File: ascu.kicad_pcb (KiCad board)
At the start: 2 copper layers, 109.6 x 35.9 mm, 91 parts, among them IC1 ATTINY25-SS, P1 B-, P10 CONN_01X01, P11 CONN_01X01, P12 CONN_01X01, P13 CONN_01X01, P14 CONN_01X01, P15 CONN_01X01, P16 CONN_01X01, P17 CONN_01X01, P18 CONN_01X01, P19 CONN_01X01, P2 B+S+, P20 CONN_01X01, P21 CONN_01X01, P22 CONN_01X01, P23 CONN_01X01, P24 CONN_01X01, P25 CONN_01X01, P26 CONN_01X01, P27 CONN_01X01, P28 CONN_01X01, P29 CONN_01X01, P3 S-, P30 CONN_01X01, P31 CONN_01X01, P32 CONN_01X01, P33 CONN_01X01, P34 CONN_01X01, P35 CONN_01X01, P37 Otwór, P38 Otwór, P39 Otwór, P4 CONN_01X01, P40 Otwór, P41 Lut, P42 Lut, P43 Lut, P44 Lut, P45 Lut, P46 Lut, P47 Lut, P48 Lut, P49 Lut, P5 CONN_01X01, P50 Lut, P51 Lut, P52 Lut, P53 Lut, P54 Lut, P55 Lut, P56 Lut, P6 CONN_01X01, P7 CONN_01X01, P8 CONN_01X01, P9 CONN_01X01, Q1 PSMN1R2, Q2 PSMN1R2, SW1 DETECT, SW3 TRIGGER, U1 SPX3819, U2 MIC4605, U3 TLP291

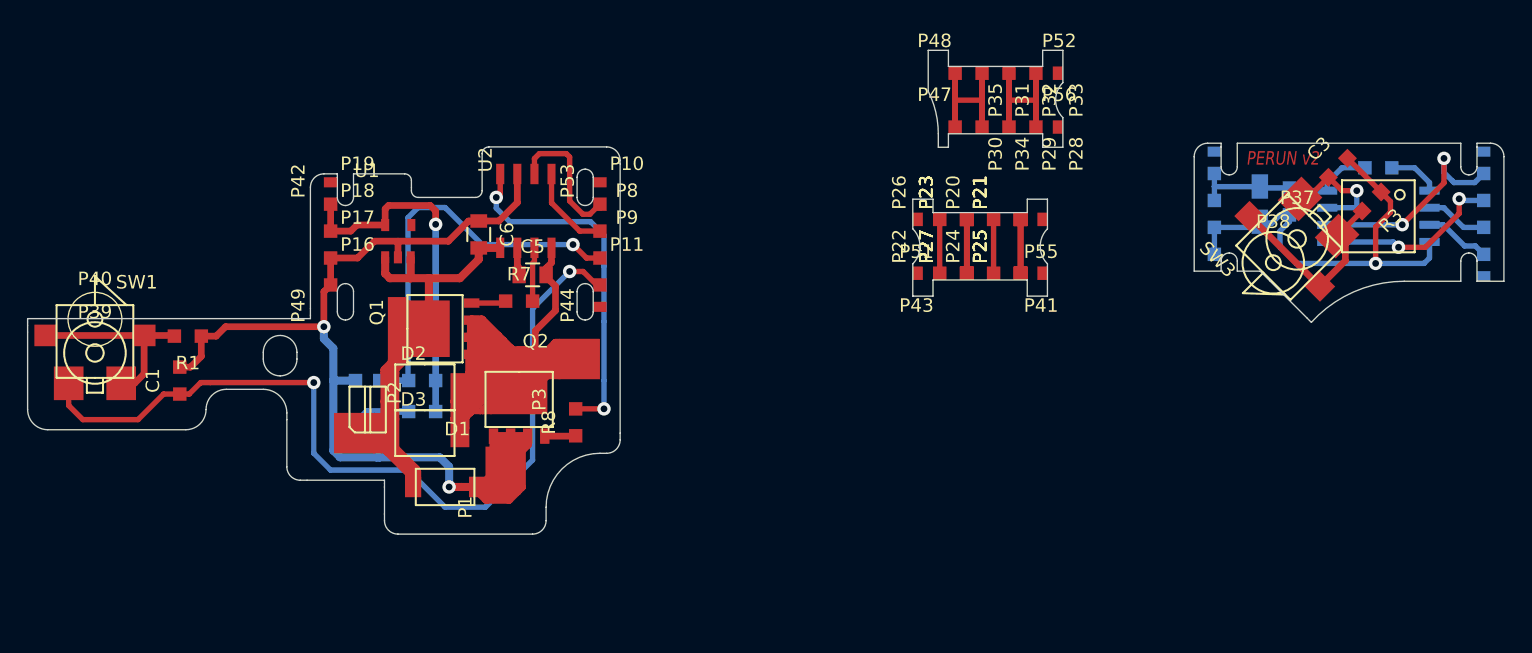
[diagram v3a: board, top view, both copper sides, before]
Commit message: Revert "Poprawki"
This reverts commit 9021c68e6a4ef5e3f9d6ce24ccd05bc863d9a415.
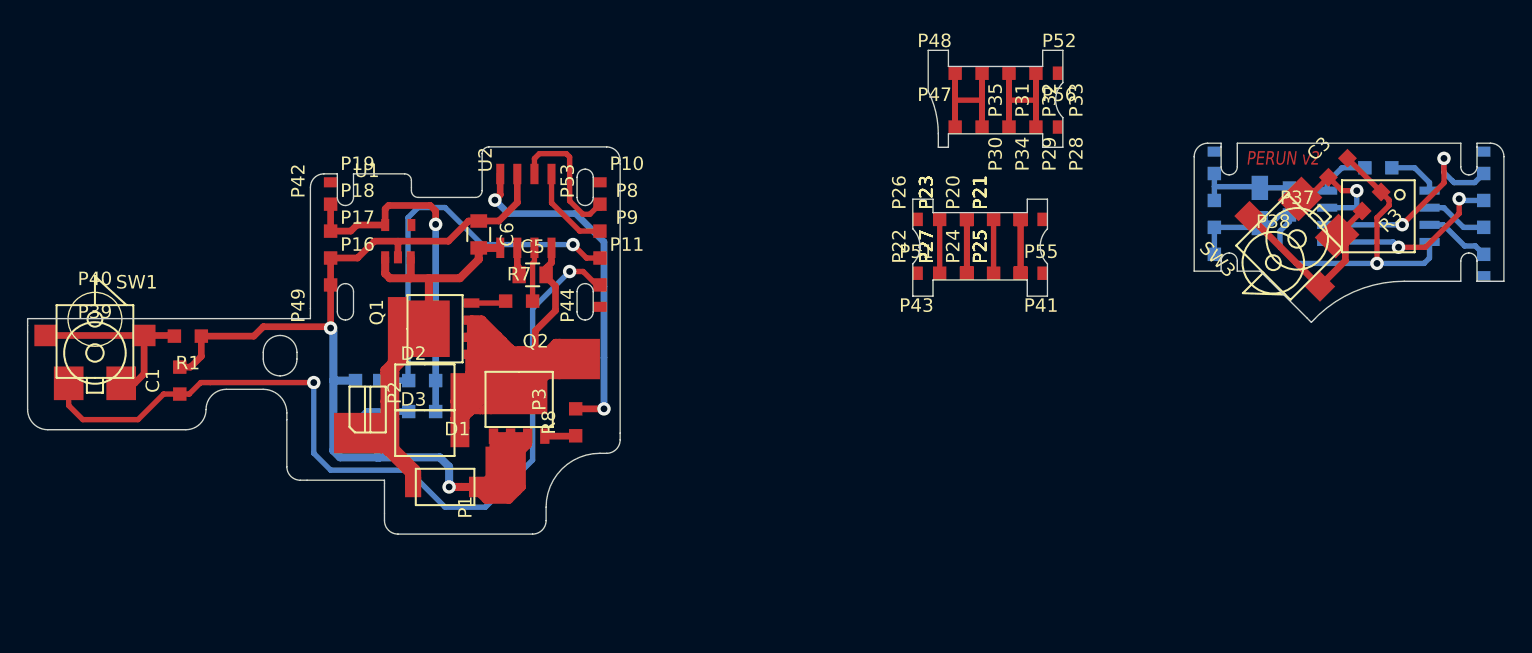
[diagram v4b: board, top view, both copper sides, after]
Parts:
- moved C2 0.10 mm to (200.5, 73.1)
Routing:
- net LO: track 26.5 -> 26.0 mm
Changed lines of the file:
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@@
     (links 93)
     (no_connects 0)
-    (area 108.899999 58.4 227.783334 97.550001)
+    (area 108.899999 58.4 198.783334 110.600001)
     (thickness 1)
     (drawings 181)
-    (tracks 478)
+    (tracks 475)
     (zones 0)
     (modules 91)
@@
   )
   (module Capacitors_Tantalum_SMD:TantalC_SizeA_EIA-3216_Reflow (layer B.Cu)
-    (at 200.5 73 270)
+    (at 200.5 73.1 270)
     (descr "Tantal Cap. , Size A, EIA-3216, Reflow")
     (tags "Tantal Capacitor Size-A EIA-3216 reflow")
@@
   (gr_line (start 128 81) (end 128 78.5) (angle 90) (layer Margin) (width 0.2))
   (gr_line (start 130 81) (end 128 81) (angle 90) (layer Margin) (width 0.2))
-  (segment (start 131 82.1) (end 131 83) (width 0.6) (layer B.Cu) (net 1))
-  (via (at 131 82.1) (size 1) (drill 0.5) (layers F.Cu B.Cu) (net 1))
-  (segment (start 131.7 83.7) (end 131.7 86.1) (width 0.6) (layer B.Cu) (net 1))
-  (segment (start 131 83) (end 131.7 83.7) (width 0.6) (layer B.Cu) (net 1))
-  (segment (start 131 82.1) (end 131 79.5) (width 0.5) (layer F.Cu) (net 1))
-  (segment (start 123 82.8) (end 123.7 82.1) (width 0.5) (layer F.Cu) (net 1))
-  (segment (start 123.7 82.1) (end 131 82.1) (width 0.5) (layer F.Cu) (net 1))
-  (segment (start 121.9 82.8) (end 123 82.8) (width 0.5) (layer F.Cu) (net 1) (status 400000))
-  (segment (start 131 79.5) (end 131.5 79) (width 0.5) (layer F.Cu) (net 1) (status 800000))
   (segment (start 120.3 85.1) (end 121.1 85.1) (width 0.5) (layer F.Cu) (net 1))
+  (segment (start 121.9 84.3) (end 121.9 82.8) (width 0.5) (layer F.Cu) (net 1))
   (segment (start 121.1 85.1) (end 121.9 84.3) (width 0.5) (layer F.Cu) (net 1))
-  (segment (start 121.9 84.3) (end 121.9 82.8) (width 0.5) (layer F.Cu) (net 1))
+  (segment (start 121.9 82.8) (end 125.8 82.8) (width 0.5) (layer F.Cu) (net 1))
+  (segment (start 131.4 82.1) (end 131.5 82.2) (width 0.5) (layer F.Cu) (net 1))
+  (segment (start 126.5 82.1) (end 131.4 82.1) (width 0.5) (layer F.Cu) (net 1))
+  (segment (start 125.8 82.8) (end 126.5 82.1) (width 0.5) (layer F.Cu) (net 1))
   (segment (start 135.15 90.4) (end 135.15 91.8) (width 0.6) (layer B.Cu) (net 1))
   (segment (start 135.15 91.8) (end 134.9 91.8) (width 0.6) (layer B.Cu) (net 1))
@@
   (segment (start 131.7 86.1) (end 131.9 86.1) (width 0.6) (layer B.Cu) (net 1))
   (segment (start 131.9 86.1) (end 131.7 86.1) (width 0.6) (layer B.Cu) (net 1))
+  (segment (start 131.5 82.2) (end 131.5 82.25) (width 0.6) (layer F.Cu) (net 1))
+  (segment (start 131.5 79) (end 131.5 82.25) (width 0.5) (layer F.Cu) (net 1))
+  (via (at 131.5 82.2) (size 1) (drill 0.5) (layers F.Cu B.Cu) (net 1))
+  (segment (start 131.7 86.1) (end 131.7 82.4) (width 0.6) (layer B.Cu) (net 1))
+  (segment (start 131.7 82.4) (end 131.5 82.2) (width 0.6) (layer B.Cu) (net 1))
   (segment (start 131.7 91.3) (end 131.7 86.1) (width 0.6) (layer B.Cu) (net 1))
+  (segment (start 134.9 91.8) (end 132.2 91.8) (width 0.6) (layer B.Cu) (net 1))
   (segment (start 132.2 91.8) (end 131.7 91.3) (width 0.6) (layer B.Cu) (net 1))
-  (segment (start 134.9 91.8) (end 132.2 91.8) (width 0.6) (layer B.Cu) (net 1))
   (segment (start 142.375 94) (end 143 94) (width 1.2) (layer F.Cu) (net 1))
   (segment (start 143 94) (end 144.5 92.5) (width 1.2) (layer F.Cu) (net 1))
@@
   (segment (start 203.656371 72.635913) (end 203.664087 72.635913) (width 0.4) (layer F.Cu) (net 11))
   (segment (start 205.5 71.995) (end 202.895 71.995) (width 0.4) (layer B.Cu) (net 12))
+  (segment (start 202.895 71.995) (end 202.7 71.8) (width 0.4) (layer B.Cu) (net 12))
   (segment (start 200.5 71.79) (end 202.69 71.79) (width 0.4) (layer B.Cu) (net 12))
+  (segment (start 202.69 71.79) (end 202.7 71.8) (width 0.4) (layer B.Cu) (net 12))
   (segment (start 197.125 71.7) (end 200.41 71.7) (width 0.4) (layer B.Cu) (net 12))
   (segment (start 200.41 71.7) (end 200.5 71.79) (width 0.4) (layer B.Cu) (net 12))
-  (segment (start 202.895 71.995) (end 202.7 71.8) (width 0.4) (layer B.Cu) (net 12))
-  (segment (start 202.69 71.79) (end 202.7 71.8) (width 0.4) (layer B.Cu) (net 12))
   (segment (start 197.125 72.725) (end 197.125 71.7) (width 0.4) (layer B.Cu) (net 12))
   (segment (start 197.125 71.7) (end 197.125 70.725) (width 0.4) (layer B.Cu) (net 12))
@@
   (segment (start 205.5 71.4) (end 205.5 71.995) (width 0.4) (layer B.Cu) (net 12))
   (segment (start 206.6 70.3) (end 205.5 71.4) (width 0.4) (layer B.Cu) (net 12))
-  (segment (start 209.507107 72.092893) (end 209.507107 72.107107) (width 0.4) (layer F.Cu) (net 13) (status C00000))
-  (segment (start 209.507107 72.107107) (end 210.2 72.8) (width 0.4) (layer F.Cu) (net 13) (status 400000))
-  (segment (start 209.1 77.4) (end 209.2 77.4) (width 0.4) (layer B.Cu) (net 13))
-  (via (at 209.1 77.4) (size 1) (drill 0.5) (layers F.Cu B.Cu) (net 13))
-  (segment (start 209.1 74.7) (end 209.1 77.4) (width 0.4) (layer F.Cu) (net 13))
-  (segment (start 210.2 73.6) (end 209.1 74.7) (width 0.4) (layer F.Cu) (net 13))
-  (segment (start 210.2 72.8) (end 210.2 73.6) (width 0.4) (layer F.Cu) (net 13))
-  (segment (start 200.5 74.41) (end 201.39 74.41) (width 0.4) (layer B.Cu) (net 13))
-  (segment (start 201.39 74.41) (end 202 73.8) (width 0.4) (layer B.Cu) (net 13))
-  (segment (start 202 73.8) (end 202.7 73.8) (width 0.4) (layer B.Cu) (net 13))
-  (segment (start 197.125 74.725) (end 200.185 74.725) (width 0.4) (layer B.Cu) (net 13))
+  (segment (start 209.507107 72.092893) (end 209.507107 72.107107) (width 0.4) (layer F.Cu) (net 13))
+  (segment (start 209.507107 72.107107) (end 210.1 72.7) (width 0.4) (layer F.Cu) (net 13))
+  (via (at 209.2 77.4) (size 1) (drill 0.5) (layers F.Cu B.Cu) (net 13))
+  (segment (start 209.2 74) (end 209.2 77.4) (width 0.4) (layer F.Cu) (net 13))
+  (segment (start 210.1 73.1) (end 209.2 74) (width 0.4) (layer F.Cu) (net 13))
+  (segment (start 210.1 72.7) (end 210.1 73.1) (width 0.4) (layer F.Cu) (net 13))
+  (segment (start 209.507107 72.092893) (end 207.007107 69.592893) (width 0.4) (layer F.Cu) (net 13))
+  (segment (start 202.7 73.8) (end 202.7 74.3) (width 0.4) (layer B.Cu) (net 13))
   (segment (start 202.7 74.3) (end 202 75) (width 0.4) (layer B.Cu) (net 13))
-  (segment (start 202 75) (end 202 76.2) (width 0.4) (layer B.Cu) (net 13))
-  (segment (start 202 76.2) (end 203.2 77.4) (width 0.4) (layer B.Cu) (net 13))
-  (segment (start 203.2 77.4) (end 209.2 77.4) (width 0.4) (layer B.Cu) (net 13))
-  (segment (start 202.7 73.8) (end 202.7 74.3) (width 0.4) (layer B.Cu) (net 13))
-  (segment (start 200.185 74.725) (end 200.5 74.41) (width 0.4) (layer B.Cu) (net 13))
-  (segment (start 209.507107 72.092893) (end 207.007107 69.592893) (width 0.4) (layer F.Cu) (net 13))
   (segment (start 213.1 77) (end 213.1 75.805) (width 0.4) (layer B.Cu) (net 13))
   (segment (start 212.7 77.4) (end 213.1 77) (width 0.4) (layer B.Cu) (net 13))
+  (segment (start 203.2 77.4) (end 209.2 77.4) (width 0.4) (layer B.Cu) (net 13))
   (segment (start 209.2 77.4) (end 212.7 77.4) (width 0.4) (layer B.Cu) (net 13))
+  (segment (start 202 76.2) (end 203.2 77.4) (width 0.4) (layer B.Cu) (net 13))
+  (segment (start 202 75) (end 202 76.2) (width 0.4) (layer B.Cu) (net 13))
+  (segment (start 200.5 74.41) (end 201.39 74.41) (width 0.4) (layer B.Cu) (net 13))
+  (segment (start 202 73.8) (end 202.7 73.8) (width 0.4) (layer B.Cu) (net 13))
+  (segment (start 201.39 74.41) (end 202 73.8) (width 0.4) (layer B.Cu) (net 13))
+  (segment (start 197.125 74.725) (end 200.185 74.725) (width 0.4) (layer B.Cu) (net 13))
+  (segment (start 200.185 74.725) (end 200.5 74.41) (width 0.4) (layer B.Cu) (net 13))
   (segment (start 197.125 76.725) (end 197.125 74.725) (width 0.4) (layer B.Cu) (net 13))
   (segment (start 213.1 73.265) (end 214.165 73.265) (width 0.4) (layer B.Cu) (net 14))
@@
   (segment (start 146.5 77.4) (end 146.5 80.2) (width 0.4) (layer F.Cu) (net 29))
   (segment (start 146.635 77.265) (end 146.5 77.4) (width 0.4) (layer F.Cu) (net 29))
-  (segment (start 149.7 88.2) (end 151.8 88.2) (width 0.4) (layer F.Cu) (net 30) (status 400000))
-  (segment (start 144.095 72.205) (end 144.095 70.76) (width 0.4) (layer F.Cu) (net 30) (status 800000))
-  (segment (start 143.8 72.5) (end 144.095 72.205) (width 0.4) (layer F.Cu) (net 30))
-  (via (at 143.8 72.5) (size 1) (drill 0.5) (layers F.Cu B.Cu) (net 30))
-  (segment (start 143.8 73.3) (end 143.8 72.5) (width 0.4) (layer B.Cu) (net 30))
-  (segment (start 144.8 74.3) (end 143.8 73.3) (width 0.4) (layer B.Cu) (net 30))
-  (segment (start 150.8 74.3) (end 144.8 74.3) (width 0.4) (layer B.Cu) (net 30))
-  (segment (start 151.8 75.3) (end 150.8 74.3) (width 0.4) (layer B.Cu) (net 30))
-  (segment (start 151.8 77.6) (end 151.8 75.3) (width 0.4) (layer B.Cu) (net 30))
-  (segment (start 151.8 81.7) (end 151.8 77.6) (width 0.4) (layer B.Cu) (net 30))
-  (segment (start 151.8 86.1) (end 151.8 81.7) (width 0.4) (layer B.Cu) (net 30))
-  (segment (start 151.8 88.2) (end 151.8 86.1) (width 0.4) (layer B.Cu) (net 30))
+  (segment (start 149.7 88.2) (end 151.8 88.2) (width 0.5) (layer F.Cu) (net 30))
+  (segment (start 144.095 72.305) (end 144.095 70.76) (width 0.5) (layer F.Cu) (net 30))
+  (segment (start 143.7 72.7) (end 144.095 72.305) (width 0.5) (layer F.Cu) (net 30))
+  (via (at 143.7 72.7) (size 1) (drill 0.5) (layers F.Cu B.Cu) (net 30))
+  (segment (start 144.7 73.7) (end 143.7 72.7) (width 0.5) (layer B.Cu) (net 30))
+  (segment (start 149.7 73.7) (end 144.7 73.7) (width 0.5) (layer B.Cu) (net 30))
+  (segment (start 151.8 75.8) (end 149.7 73.7) (width 0.5) (layer B.Cu) (net 30))
+  (segment (start 151.8 79.1) (end 151.8 75.8) (width 0.5) (layer B.Cu) (net 30))
+  (segment (start 151.8 84.4) (end 151.8 79.1) (width 0.5) (layer B.Cu) (net 30))
+  (segment (start 151.8 88.2) (end 151.8 84.4) (width 0.5) (layer B.Cu) (net 30))
   (via (at 151.8 88.2) (size 1) (drill 0.5) (layers F.Cu B.Cu) (net 30))
   (zone (net 0) (net_name "") (layer B.Paste) (hatch none 0.508)
